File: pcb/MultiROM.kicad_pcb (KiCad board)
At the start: 2 copper layers, 85.1 x 62.9 mm, 7 parts, among them J1 Conn_02x22_Row_Letter_First, SW1 SW_DIP_x04, U1 SST39SF010, U2 GAL16V8

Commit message: PCB+netlist tidyup
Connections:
- net /CS_R~{W} renamed /R~{W}_{E}_CS_{M}
- net /M_R~{W} renamed /R~{W}_{M}
- RN1 pad 3: /~{Lo_A15} -> /~{Lo_A16}
- RN1 pad 4: /~{Lo_A16} -> /~{Lo_A15}
- RN1 pad 5: /~{Hi_A15} -> /~{Hi_A16}
- RN1 pad 6: /~{Hi_A16} -> /~{Hi_A15}
- SW1 pad 1: /~{Lo_A15} -> /~{Lo_A16}
- SW1 pad 2: /~{Lo_A16} -> /~{Lo_A15}
- SW1 pad 3: /~{Hi_A15} -> /~{Hi_A16}
- SW1 pad 4: /~{Hi_A16} -> /~{Hi_A15}
- U2 pad 6: /~{Hi_A16} -> /~{Hi_A15}
- U2 pad 7: /~{Hi_A15} -> /~{Hi_A16}
- U2 pad 8: /~{Lo_A16} -> /~{Lo_A15}
- U2 pad 9: /~{Lo_A15} -> /~{Lo_A16}
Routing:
- net /~{Hi_A16}: track 36.0 -> 32.4 mm
- net /~{Hi_A15}: track 32.4 -> 36.0 mm
- net /~{Lo_A16}: track 28.8 -> 26.1 mm
- net /~{Lo_A15}: track 26.1 -> 28.8 mm

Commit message: Placeholder text for fab info
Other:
- board text added: "${PCBFab_placeholder}"
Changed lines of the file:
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@@
     )
   )
+  (property "PCBFab_placeholder" "")
   (net 0 "")
   (net 1 "GND")
@@
   (gr_line (start 111.125 76.2) (end 97.79 76.2)
     (stroke (width 0.1) (type solid)) (layer "Edge.Cuts"))
+  (gr_text "${PCBFab_placeholder}" (at 81.788 54.864 270) (layer "B.SilkS")
+    (effects (font (size 1 1) (thickness 0.15)) (justify left bottom mirror))
+  )
   (gr_text "This side to rear" (at 110.49 28.575) (layer "B.SilkS")
     (effects (font (size 1.25 1.25) (thickness 0.1875)) (justify left bottom mirror))

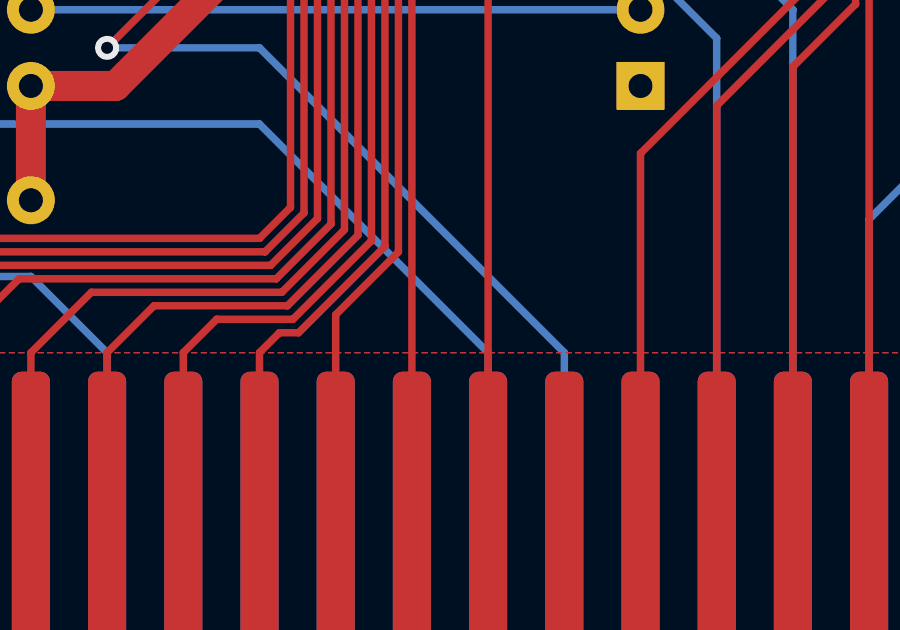
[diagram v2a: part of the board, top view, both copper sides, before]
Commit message: Rename cartridge footprint+library to avoid spaces
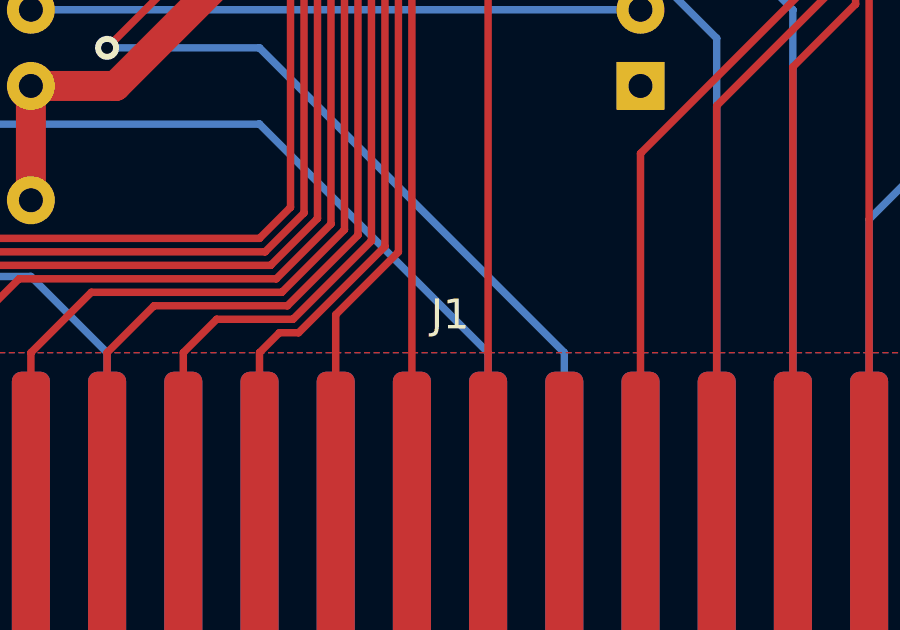
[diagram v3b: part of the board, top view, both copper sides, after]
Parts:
- J1: footprint BBC Master Cartridge:BBC Master Cartridge -> BBC Master / Acorn Electron Cartridge:bbc-master-acorn-electron-cartridge
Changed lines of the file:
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@@
     )
   )
-  (footprint "BBC Master Cartridge:BBC Master Cartridge" (layer "F.Cu")
+  (footprint "BBC Master / Acorn Electron Cartridge:bbc-master-acorn-electron-cartridge" (layer "F.Cu")
     (at 68.58 76.5175)
     (property "Sheetfile" "MultiROM.kicad_sch")
@@
     (property "ki_keywords" "connector")
     (attr through_hole)
-    (fp_text reference "J1" (at 0 -1.5875) (layer "F.SilkS") hide
+    (fp_text reference "J1" (at 0 -1.5875) (layer "F.SilkS")
         (effects (font (size 1 1) (thickness 0.15)))
     )
-    (fp_text value "Conn_02x22_Row_Letter_First" (at 0 -4.1275) (layer "F.Fab") hide
+    (fp_text value "Conn_02x22_Row_Letter_First" (at 0 -4.1275) (layer "F.Fab")
         (effects (font (size 1 1) (thickness 0.15)))
     )

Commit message: Build system
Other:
- board text added: "github.com/rhalkyard/bbc-multirom ${VERSION}"
- board text removed: "github.com/rhalkyard/bbc-multirom Issue 1"
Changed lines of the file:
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@@
   (title_block
     (title "Cartridge for BBC Master & Acorn Electron")
+    (date "2023-03-18")
+    (rev "${VERSION}")
   )
   (layers
@@
   )
   (property "PCBFab_placeholder" "")
+  (property "VERSION" "(NO VERSION)")
   (net 0 "")
   (net 1 "GND")
@@
     (pad "8" thru_hole oval (at 7.62 0 90) (size 1.6 1.6) (drill 0.8) (layers "*.Cu" "*.Mask")
       (net 1 "GND") (pintype "passive"))
-    (model "${KICAD6_3DMODEL_DIR}/Button_Switch_THT.3dshapes/SW_DIP_SPSTx04_Slide_9.78x12.34mm_W7.62mm_P2.54mm.wrl"
+    (model "${KICAD7_3DMODEL_DIR}/Button_Switch_THT.3dshapes/SW_DIP_SPSTx04_Slide_9.78x12.34mm_W7.62mm_P2.54mm.wrl"
       (offset (xyz 0 0 0))
       (scale (xyz 1 1 1))
@@
     (pad "2" thru_hole circle (at 2.5 0 180) (size 1.6 1.6) (drill 0.8) (layers "*.Cu" "*.Mask")
       (net 1 "GND") (pintype "passive"))
-    (model "${KICAD6_3DMODEL_DIR}/Capacitor_THT.3dshapes/C_Disc_D3.0mm_W1.6mm_P2.50mm.wrl"
+    (model "${KICAD7_3DMODEL_DIR}/Capacitor_THT.3dshapes/C_Disc_D3.0mm_W1.6mm_P2.50mm.wrl"
       (offset (xyz 0 0 0))
       (scale (xyz 1 1 1))
@@
     (pad "20" thru_hole oval (at 7.62 0) (size 1.6 1.6) (drill 0.8) (layers "*.Cu" "*.Mask")
       (net 2 "VCC") (pinfunction "VCC") (pintype "power_in"))
-    (model "${KICAD6_3DMODEL_DIR}/Package_DIP.3dshapes/DIP-20_W7.62mm.wrl"
+    (model "${KICAD7_3DMODEL_DIR}/Package_DIP.3dshapes/DIP-20_W7.62mm.wrl"
       (offset (xyz 0 0 0))
       (scale (xyz 1 1 1))
@@
     (pad "6" thru_hole oval (at 12.7 0 270) (size 1.6 1.6) (drill 0.8) (layers "*.Cu" "*.Mask")
       (net 44 "/~{Hi_A15}") (pinfunction "R5") (pintype "passive"))
-    (model "${KICAD6_3DMODEL_DIR}/Resistor_THT.3dshapes/R_Array_SIP6.wrl"
+    (model "${KICAD7_3DMODEL_DIR}/Resistor_THT.3dshapes/R_Array_SIP6.wrl"
       (offset (xyz 0 0 0))
       (scale (xyz 1 1 1))
@@
     (pad "32" thru_hole oval (at 15.24 0) (size 1.6 1.6) (drill 0.8) (layers "*.Cu" "*.Mask")
       (net 2 "VCC") (pinfunction "VCC") (pintype "power_in"))
-    (model "${KICAD6_3DMODEL_DIR}/Package_DIP.3dshapes/DIP-32_W15.24mm.wrl"
+    (model "${KICAD7_3DMODEL_DIR}/Package_DIP.3dshapes/DIP-32_W15.24mm.wrl"
       (offset (xyz 0 0 0))
       (scale (xyz 1 1 1))
@@
     (pad "2" thru_hole circle (at 2.5 0 180) (size 1.6 1.6) (drill 0.8) (layers "*.Cu" "*.Mask")
       (net 1 "GND") (pintype "passive"))
-    (model "${KICAD6_3DMODEL_DIR}/Capacitor_THT.3dshapes/C_Disc_D3.0mm_W1.6mm_P2.50mm.wrl"
+    (model "${KICAD7_3DMODEL_DIR}/Capacitor_THT.3dshapes/C_Disc_D3.0mm_W1.6mm_P2.50mm.wrl"
       (offset (xyz 0 0 0))
       (scale (xyz 1 1 1))
@@
     (effects (font (size 3 3) (thickness 0.6) bold italic) (justify left bottom))
   )
-  (gr_text "github.com/rhalkyard/bbc-multirom\nIssue 1" (at 36.195 57.785 90) (layer "F.SilkS")
+  (gr_text "github.com/rhalkyard/bbc-multirom\n${VERSION}" (at 36.195 57.785 90) (layer "F.SilkS")
     (effects (font (size 1 1) (thickness 0.125)) (justify left top))
   )
